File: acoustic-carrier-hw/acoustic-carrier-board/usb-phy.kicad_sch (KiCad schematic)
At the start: 51 parts, among them J801 TYPE-C-31-M-12, U801 USB3300-EZK, U802 LMV321, Y801 Crystal_GND24_Small

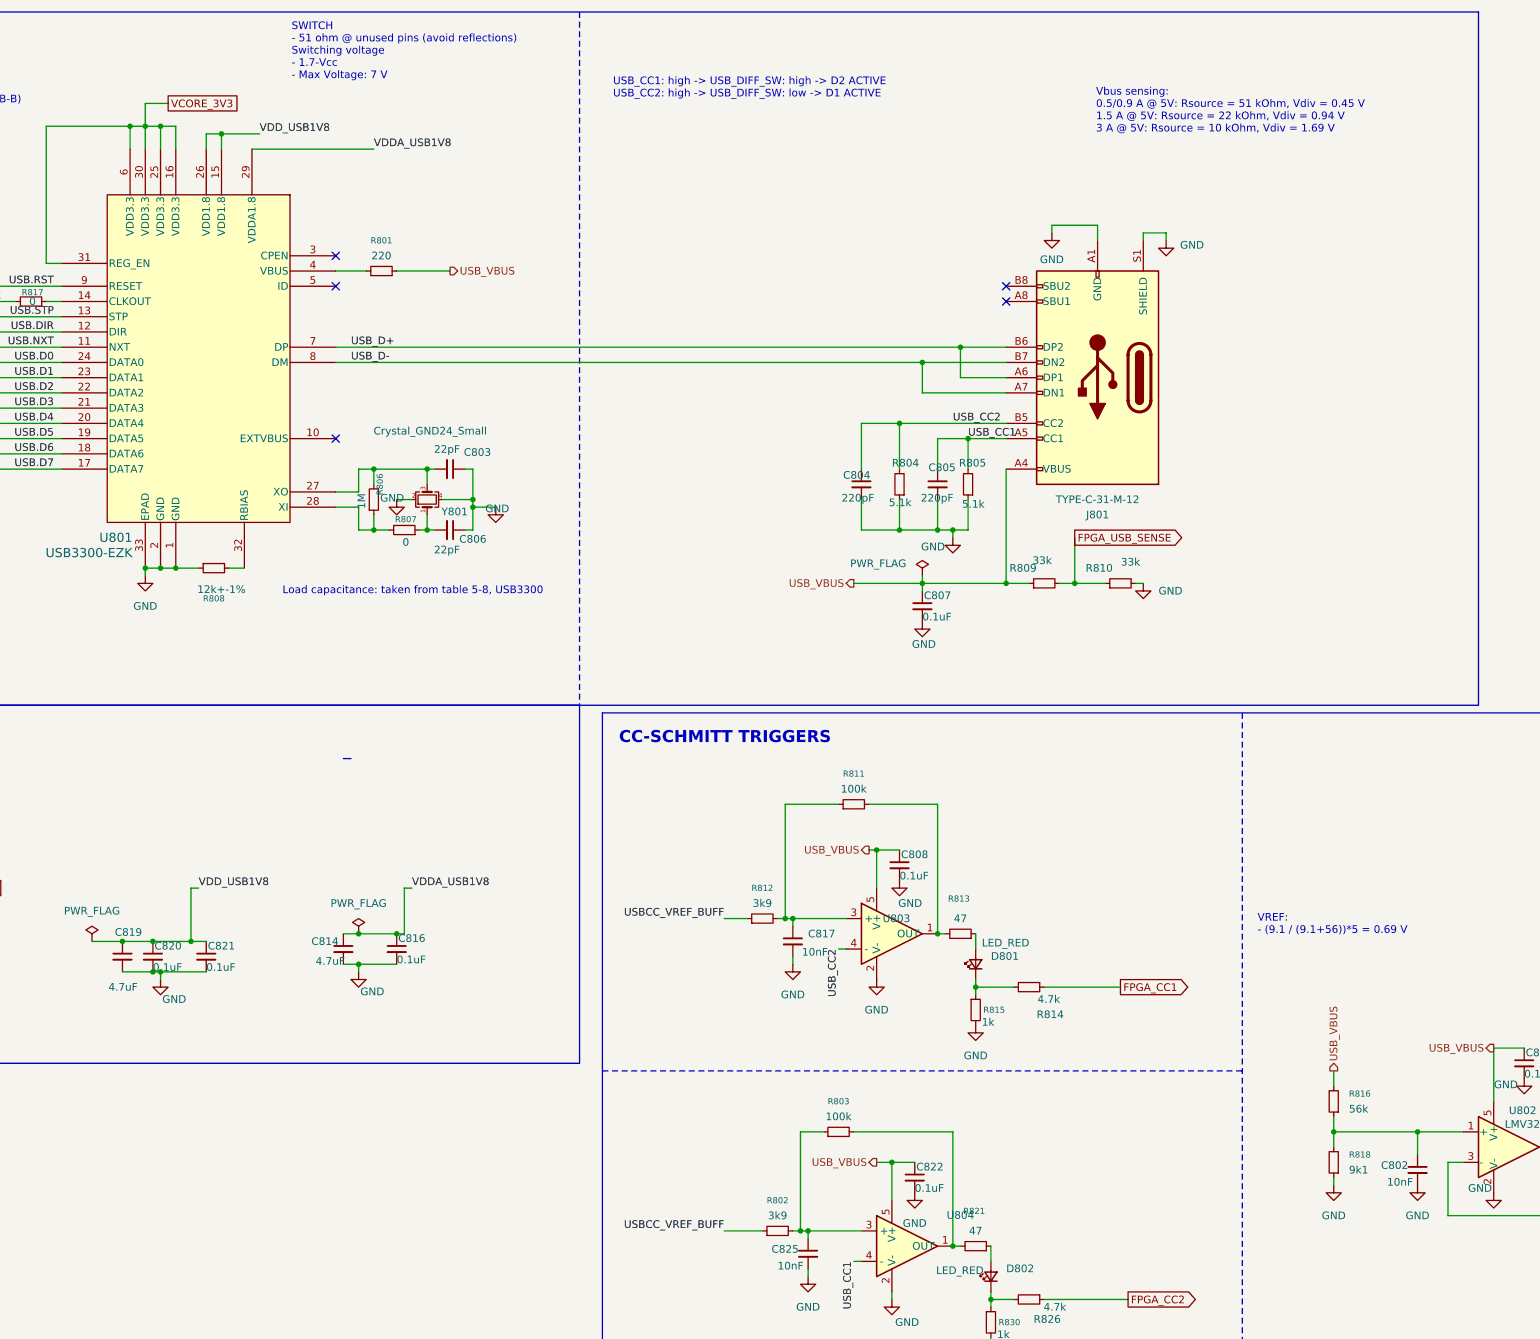
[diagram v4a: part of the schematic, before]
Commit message: [carrier] finished for production (next) reroute the LPDDR3, with appropriate CMD-CTRL bus delays, and change banks for command-control
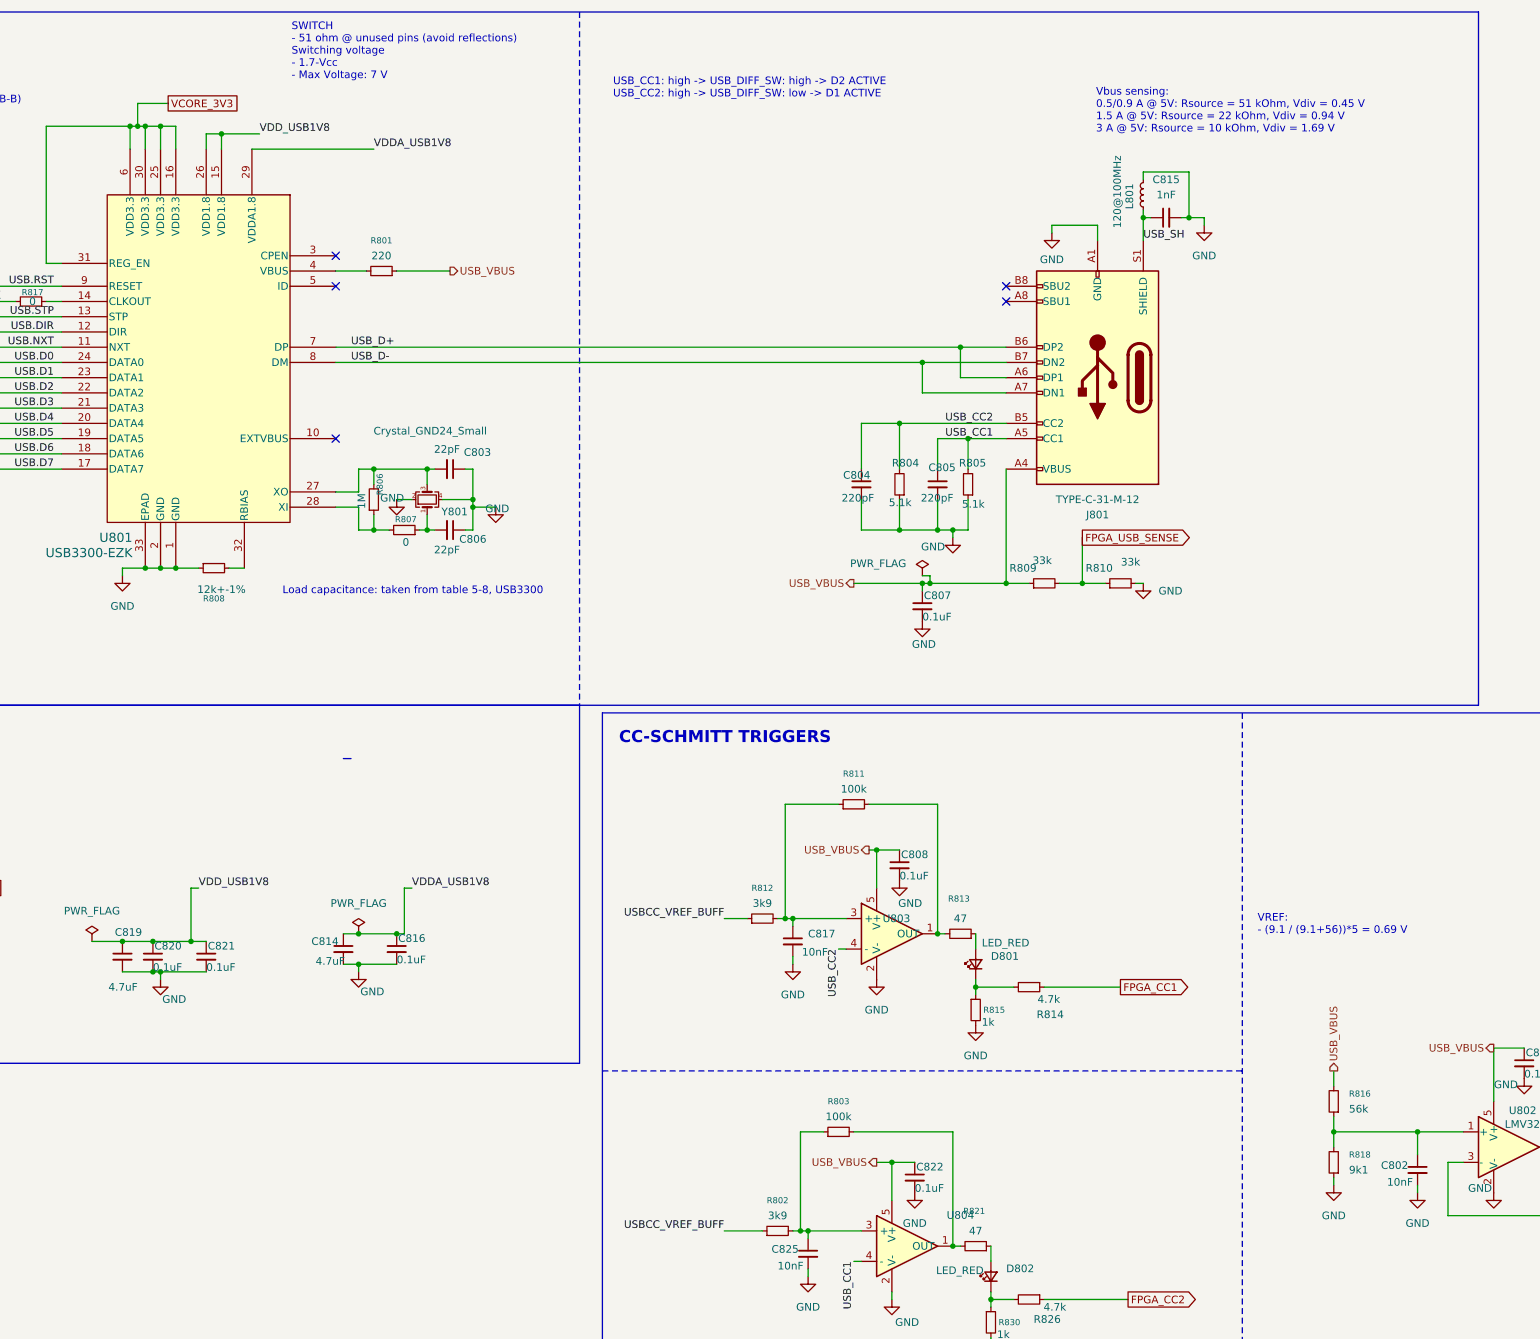
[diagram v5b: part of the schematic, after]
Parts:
- added C815: 1nF, Capacitor_SMD:C_1206_3216Metric, symbol Device:C_Small
- added L801: 120@100MHz, Inductor_SMD:L_0603_1608Metric, symbol Device:L_Small
- R804, R805: Manufacturing part number 0805W8F5101T5E -> (none)
- R810: Manufacturing part number 0603WAF3302T5E -> (none)
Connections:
- net GND: now also C815.2, L801.1; no longer J801.S1 (SHIELD)
- new net USB_SH: C815.1, J801.S1 (SHIELD), L801.2
